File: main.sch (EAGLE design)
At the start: 6 parts

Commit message: Test layout for proto PCB of 10x28 holes.
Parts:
- R1, R2: device resistor:R-EU_0411/15 -> resistor:R-EU_0204/7
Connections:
- net GND: now also S1_RESET.P1, S2_PROG.S1
- net N$3: now also S2_PROG.P1
- net N$7: now also S1_RESET.S1
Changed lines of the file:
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@@
 <grid distance="0.1" unitdist="inch" unit="inch" style="lines" multiple="1" display="no" altdistance="0.01" altunitdist="inch" altunit="inch"/>
 <layers>
-<layer number="1" name="Top" color="4" fill="1" visible="no" active="no"/>
-<layer number="16" name="Bottom" color="1" fill="1" visible="no" active="no"/>
-<layer number="17" name="Pads" color="2" fill="1" visible="no" active="no"/>
-<layer number="18" name="Vias" color="2" fill="1" visible="no" active="no"/>
-<layer number="19" name="Unrouted" color="6" fill="1" visible="no" active="no"/>
-<layer number="20" name="Dimension" color="15" fill="1" visible="no" active="no"/>
-<layer number="21" name="tPlace" color="7" fill="1" visible="no" active="no"/>
-<layer number="22" name="bPlace" color="7" fill="1" visible="no" active="no"/>
-<layer number="23" name="tOrigins" color="15" fill="1" visible="no" active="no"/>
-<layer number="24" name="bOrigins" color="15" fill="1" visible="no" active="no"/>
-<layer number="25" name="tNames" color="7" fill="1" visible="no" active="no"/>
-<layer number="26" name="bNames" color="7" fill="1" visible="no" active="no"/>
-<layer number="27" name="tValues" color="7" fill="1" visible="no" active="no"/>
-<layer number="28" name="bValues" color="7" fill="1" visible="no" active="no"/>
+<layer number="1" name="Top" color="4" fill="1" visible="yes" active="no"/>
+<layer number="16" name="Bottom" color="1" fill="1" visible="yes" active="no"/>
+<layer number="17" name="Pads" color="2" fill="1" visible="yes" active="no"/>
+<layer number="18" name="Vias" color="2" fill="1" visible="yes" active="no"/>
+<layer number="19" name="Unrouted" color="6" fill="1" visible="yes" active="no"/>
+<layer number="20" name="Dimension" color="15" fill="1" visible="yes" active="no"/>
+<layer number="21" name="tPlace" color="7" fill="1" visible="yes" active="no"/>
+<layer number="22" name="bPlace" color="7" fill="1" visible="yes" active="no"/>
+<layer number="23" name="tOrigins" color="15" fill="1" visible="yes" active="no"/>
+<layer number="24" name="bOrigins" color="15" fill="1" visible="yes" active="no"/>
+<layer number="25" name="tNames" color="7" fill="1" visible="yes" active="no"/>
+<layer number="26" name="bNames" color="7" fill="1" visible="yes" active="no"/>
+<layer number="27" name="tValues" color="7" fill="1" visible="yes" active="no"/>
+<layer number="28" name="bValues" color="7" fill="1" visible="yes" active="no"/>
 <layer number="29" name="tStop" color="7" fill="3" visible="no" active="no"/>
 <layer number="30" name="bStop" color="7" fill="6" visible="no" active="no"/>
@@
 <layer number="35" name="tGlue" color="7" fill="4" visible="no" active="no"/>
 <layer number="36" name="bGlue" color="7" fill="5" visible="no" active="no"/>
-<layer number="37" name="tTest" color="7" fill="1" visible="no" active="no"/>
-<layer number="38" name="bTest" color="7" fill="1" visible="no" active="no"/>
+<layer number="37" name="tTest" color="7" fill="1" visible="yes" active="no"/>
+<layer number="38" name="bTest" color="7" fill="1" visible="yes" active="no"/>
 <layer number="39" name="tKeepout" color="4" fill="11" visible="no" active="no"/>
 <layer number="40" name="bKeepout" color="1" fill="11" visible="no" active="no"/>
@@
 <layer number="44" name="Drills" color="7" fill="1" visible="no" active="no"/>
 <layer number="45" name="Holes" color="7" fill="1" visible="no" active="no"/>
-<layer number="46" name="Milling" color="3" fill="1" visible="no" active="no"/>
-<layer number="47" name="Measures" color="7" fill="1" visible="no" active="no"/>
-<layer number="48" name="Document" color="7" fill="1" visible="no" active="no"/>
-<layer number="49" name="Reference" color="7" fill="1" visible="no" active="no"/>
-<layer number="51" name="tDocu" color="7" fill="1" visible="no" active="no"/>
-<layer number="52" name="bDocu" color="7" fill="1" visible="no" active="no"/>
+<layer number="46" name="Milling" color="3" fill="1" visible="yes" active="no"/>
+<layer number="47" name="Measures" color="7" fill="1" visible="yes" active="no"/>
+<layer number="48" name="Document" color="7" fill="1" visible="yes" active="no"/>
+<layer number="49" name="Reference" color="7" fill="1" visible="yes" active="no"/>
+<layer number="51" name="tDocu" color="7" fill="1" visible="yes" active="no"/>
+<layer number="52" name="bDocu" color="7" fill="1" visible="yes" active="no"/>
 <layer number="90" name="Modules" color="5" fill="1" visible="yes" active="yes"/>
 <layer number="91" name="Nets" color="2" fill="1" visible="yes" active="yes"/>
@@
 <part name="S1_RESET" library="switch-omron" deviceset="10-XX" device=""/>
 <part name="S2_PROG" library="switch-omron" deviceset="10-XX" device=""/>
-<part name="R1" library="resistor" deviceset="R-EU_" device="0411/15"/>
-<part name="R2" library="resistor" deviceset="R-EU_" device="0411/15"/>
+<part name="R1" library="resistor" deviceset="R-EU_" device="0204/7"/>
+<part name="R2" library="resistor" deviceset="R-EU_" device="0204/7"/>
 <part name="FTDI" library="con-lstb" deviceset="MA06-1" device=""/>
 </parts>
@@
 <junction x="96.52" y="45.72"/>
 <label x="96.52" y="45.72" size="1.016" layer="95" xref="yes"/>
+<pinref part="S1_RESET" gate="1" pin="P1"/>
+<wire x1="96.52" y1="45.72" x2="96.52" y2="48.26" width="0.1524" layer="91"/>
+<junction x="96.52" y="48.26"/>
 </segment>
 <segment>
@@
 <junction x="22.86" y="53.34"/>
 <label x="22.86" y="53.34" size="1.016" layer="95" rot="R180" xref="yes"/>
+<pinref part="S2_PROG" gate="1" pin="S1"/>
+<junction x="22.86" y="55.88"/>
+<wire x1="22.86" y1="55.88" x2="22.86" y2="53.34" width="0.1524" layer="91"/>
 </segment>
 </net>
@@
 <junction x="33.02" y="53.34"/>
 <wire x1="43.18" y1="53.34" x2="33.02" y2="53.34" width="0.1524" layer="91"/>
+<pinref part="S2_PROG" gate="1" pin="P1"/>
+<junction x="33.02" y="55.88"/>
+<wire x1="33.02" y1="53.34" x2="33.02" y2="55.88" width="0.1524" layer="91"/>
 </segment>
 </net>
@@
 <junction x="86.36" y="45.72"/>
 <wire x1="83.82" y1="45.72" x2="86.36" y2="45.72" width="0.1524" layer="91"/>
-</segment>
-</net>
+<pinref part="S1_RESET" gate="1" pin="S1"/>
+<wire x1="86.36" y1="45.72" x2="86.36" y2="48.26" width="0.1524" layer="91"/>
+<junction x="86.36" y="48.26"/>
+</segment>
+</net>

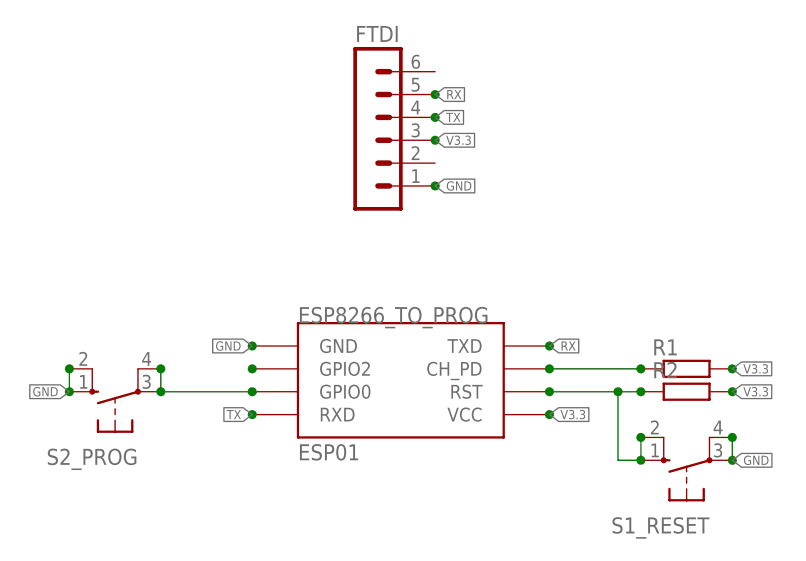
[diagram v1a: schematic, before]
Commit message: Fix unused tracks, added R values.
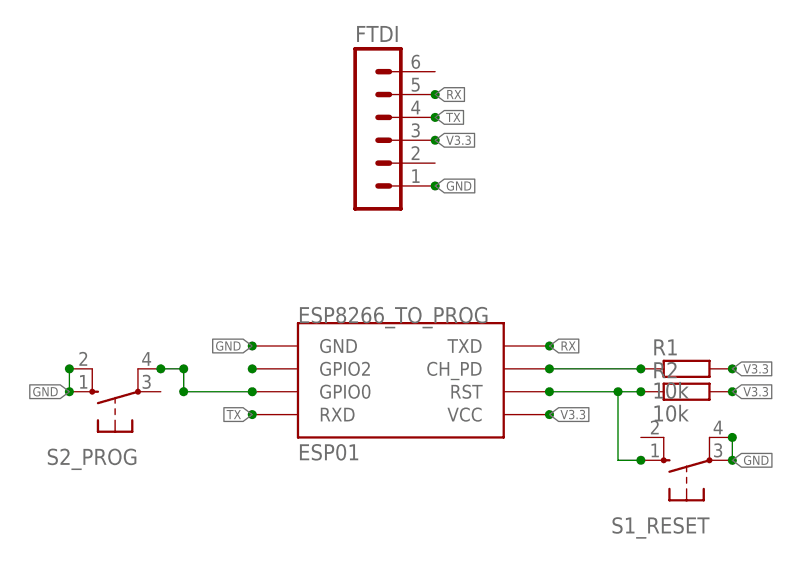
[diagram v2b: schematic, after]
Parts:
- R1, R2: value (none) -> 10k
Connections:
- net N$3: no longer S2_PROG.P
- net N$7: no longer S1_RESET.S1
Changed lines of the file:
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@@
 <part name="S1_RESET" library="switch-omron" deviceset="10-XX" device=""/>
 <part name="S2_PROG" library="switch-omron" deviceset="10-XX" device=""/>
-<part name="R1" library="resistor" deviceset="R-EU_" device="0204/7"/>
-<part name="R2" library="resistor" deviceset="R-EU_" device="0204/7"/>
+<part name="R1" library="resistor" deviceset="R-EU_" device="0204/7" value="10k"/>
+<part name="R2" library="resistor" deviceset="R-EU_" device="0204/7" value="10k"/>
 <part name="FTDI" library="con-lstb" deviceset="MA06-1" device=""/>
 </parts>
@@
 <pinref part="ESP8266_TO_PROG" gate="G$1" pin="GPIO0"/>
 <junction x="43.18" y="53.34"/>
-<pinref part="S2_PROG" gate="1" pin="P"/>
-<junction x="33.02" y="53.34"/>
-<wire x1="43.18" y1="53.34" x2="33.02" y2="53.34" width="0.1524" layer="91"/>
+<wire x1="43.18" y1="53.34" x2="35.56" y2="53.34" width="0.1524" layer="91"/>
 <pinref part="S2_PROG" gate="1" pin="P1"/>
+<wire x1="33.02" y1="55.88" x2="35.56" y2="55.88" width="0.1524" layer="91"/>
+<wire x1="35.56" y1="55.88" x2="35.56" y2="53.34" width="0.1524" layer="91"/>
 <junction x="33.02" y="55.88"/>
-<wire x1="33.02" y1="53.34" x2="33.02" y2="55.88" width="0.1524" layer="91"/>
+<junction x="35.56" y="53.34"/>
+<junction x="35.56" y="55.88"/>
 </segment>
 </net>
@@
 <wire x1="83.82" y1="53.34" x2="83.82" y2="45.72" width="0.1524" layer="91"/>
 <pinref part="S1_RESET" gate="1" pin="S"/>
+<wire x1="83.82" y1="45.72" x2="86.36" y2="45.72" width="0.1524" layer="91"/>
 <junction x="86.36" y="45.72"/>
-<wire x1="83.82" y1="45.72" x2="86.36" y2="45.72" width="0.1524" layer="91"/>
-<pinref part="S1_RESET" gate="1" pin="S1"/>
-<wire x1="86.36" y1="45.72" x2="86.36" y2="48.26" width="0.1524" layer="91"/>
-<junction x="86.36" y="48.26"/>
 </segment>
 </net>
